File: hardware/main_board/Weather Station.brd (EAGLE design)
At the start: 55.5 x 44.4 mm, 34 parts, among them J2 RJ12, Q1 200mA/40V, Q2 220mA/50V/3.5Ω, U1 328P, U2 MCP1703T-3302E/CB, U3 W25X40CLSNIG, X2 B2B-PH-K-S, X3 B2B-XH-2, Y1 8MHz

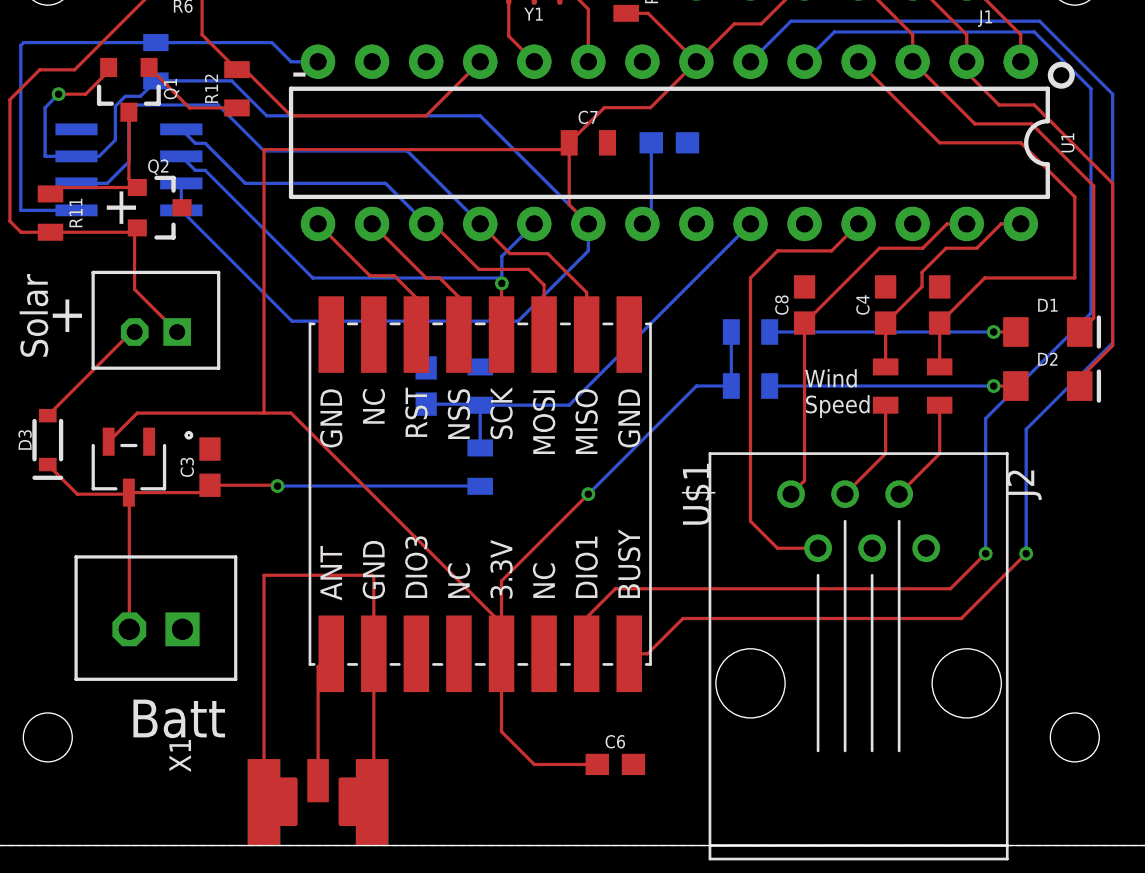
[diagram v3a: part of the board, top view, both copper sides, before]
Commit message: Added stationID to EEPROM and made changeable. Some hardware work.
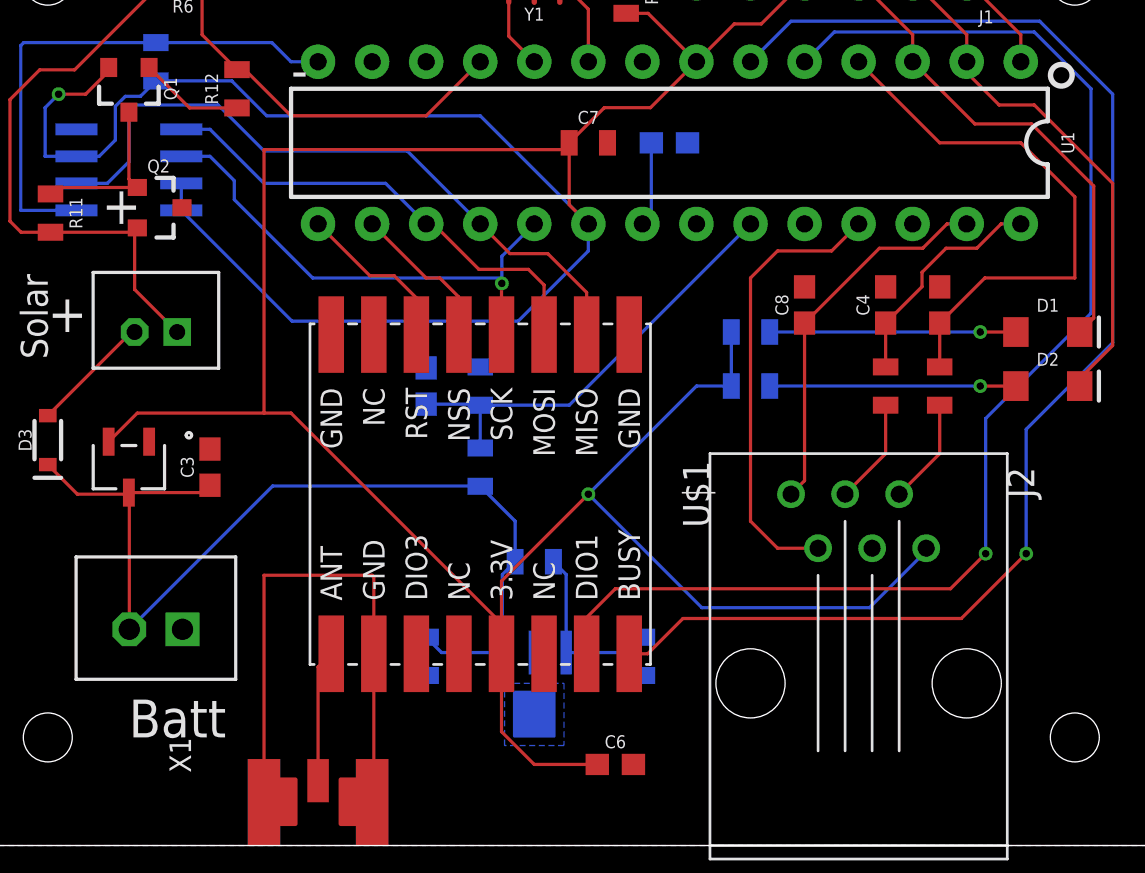
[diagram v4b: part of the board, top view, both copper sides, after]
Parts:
- added C9: 22uF, SparkFun-Capacitors:0805
- added R13, R7: (no value), SparkFun-Resistors:0805
- added U4: TL431BQPK, my-components:PK3
- C3: value 1.0uF -> 10uF
- R12: value 1k -> 33k
- R6: value 100k -> 10k
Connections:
- new net N$1: R13.1, R7.2, U4.3
- net GND: now also C9.2, R13.2, U4.2, U4.A2
- net VCC: now also J2.6
- net VIN: now also C9.1, R7.1, U4.1
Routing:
- net VCC: track 166.0 -> 185.3 mm
- net VIN: track 27.5 -> 46.7 mm, vias 1 -> 0
- net N$1: track 0.00 -> 8.39 mm
- net SCK: track 23.3 -> 23.8 mm
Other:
- board text added: "GND"
- board text added: "Sense Switch"
- board text added: "Shunt Voltage Reg"
- board text added: "Temp"
- board text added: "VCC"
- board text added: "Wind Dir"
- board text added: "Wind Spd"
- board text removed: "Wind Speed"

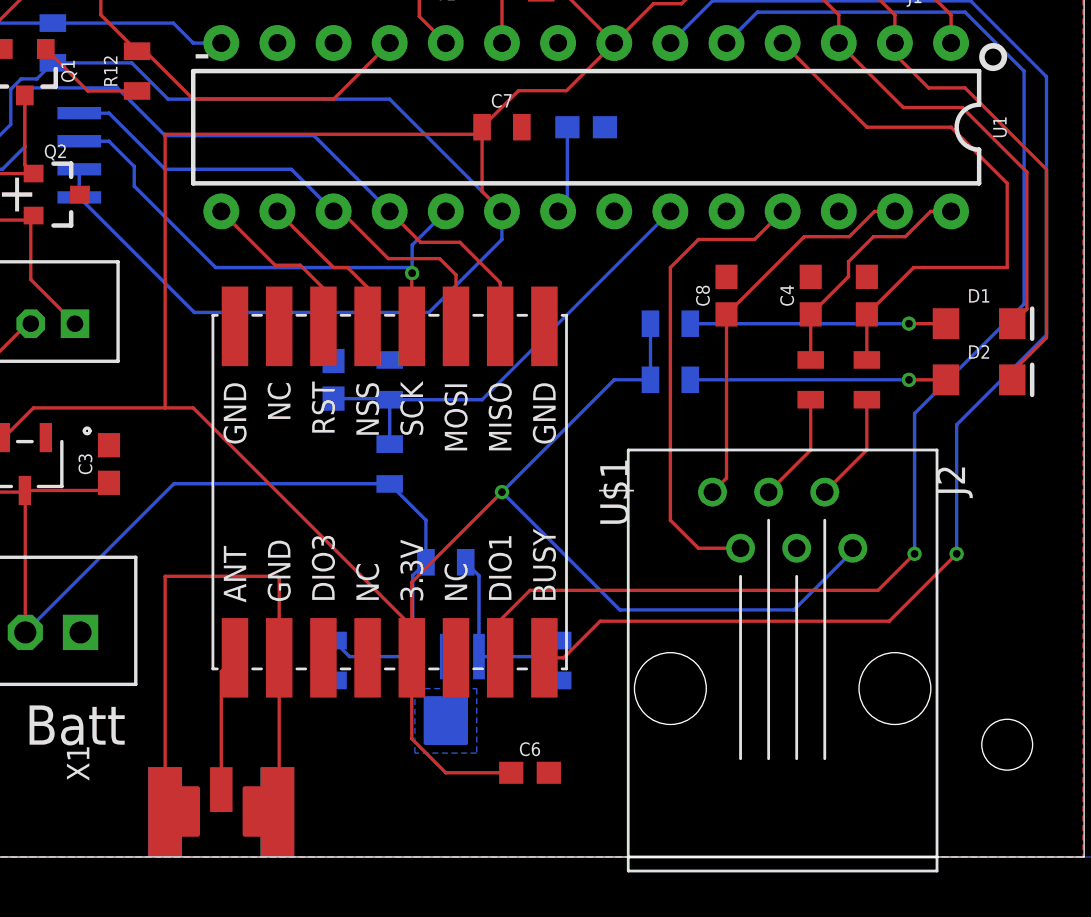
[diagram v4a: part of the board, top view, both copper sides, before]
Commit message: Switched to DRF126xT module
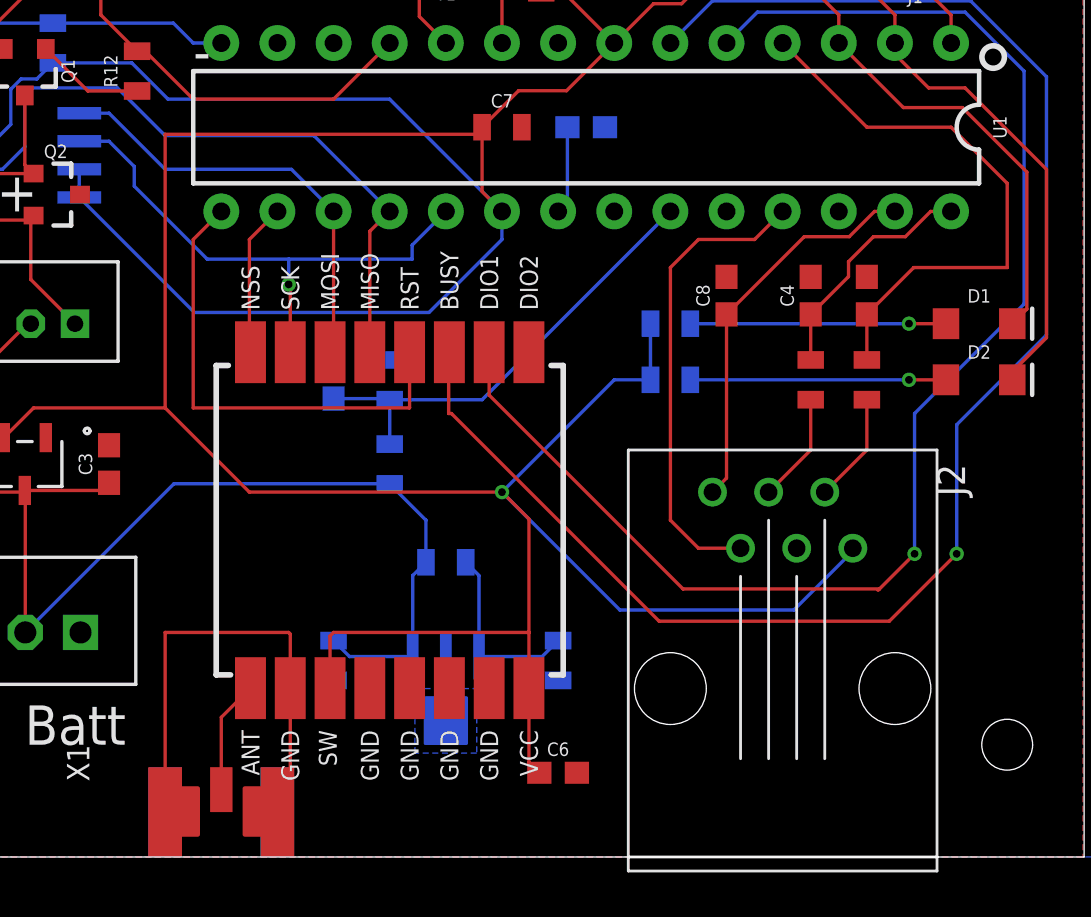
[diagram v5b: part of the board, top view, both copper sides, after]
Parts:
- U$1: value NICERF_SX1268 -> SX1262; device diy-modules:WIRELESS-LORA-NICERF1268 -> RadioShield:SX1262
- moved U$1 1.27 mm to (24.1, 15.2), turned to 90 degrees
- moved C6 1.27 mm to (31.8, 3.81)
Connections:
- net ANT: now also U$1.ANT; no longer U$1.B8
- net BUSY: now also U$1.BUSY; no longer U$1.B1
- net DIO1: now also U$1.DIO1; no longer U$1.B2
- net GND: now also U$1.GND@2, U$1.GND@3, U$1.GND@4, U$1.GND@5; no longer U$1.A1, U$1.A8
- net MISO: now also U$1.MISO; no longer U$1.A2
- net MOSI: now also U$1.MOSI; no longer U$1.A3
- net RF_GND: now also U$1.GND@1; no longer U$1.B7
- net SCK: now also U$1.SCK; no longer U$1.A4
- net SX_NSS: now also U$1.NSS; no longer U$1.A5
- net SX_RST: now also U$1.RST; no longer U$1.A6
- net VCC: now also U$1.SW, U$1.VCC; no longer U$1.B4
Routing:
- net SX_RST: track 7.78 -> 21.7 mm
- net BUSY: track 63.1 -> 73.4 mm
- net VCC: track 185.3 -> 191.7 mm
- net RF_GND: track 26.5 -> 22.1 mm
- net DIO1: track 60.7 -> 64.6 mm
- net MOSI: track 22.4 -> 20.1 mm
- net MISO: track 32.7 -> 31.1 mm
- net ANT: track 6.22 -> 5.14 mm
- net SCK: track 23.8 -> 24.8 mm

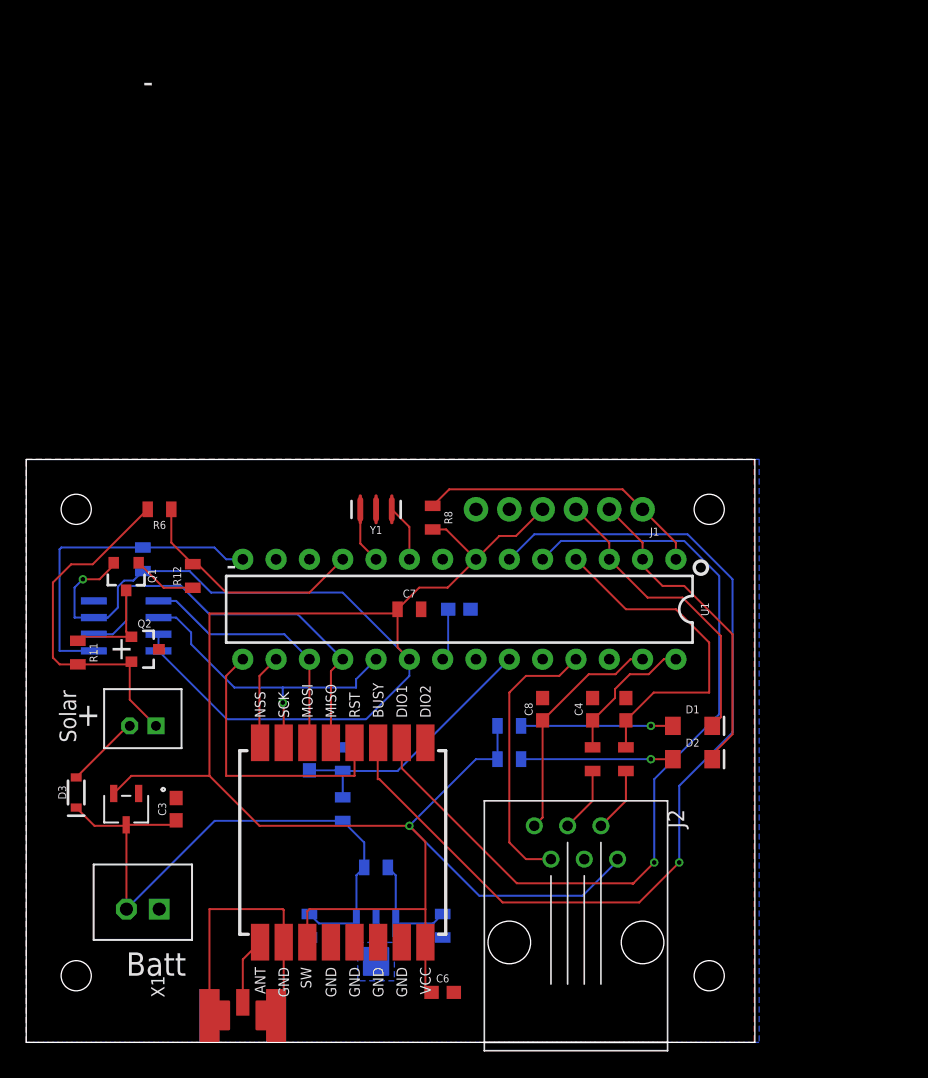
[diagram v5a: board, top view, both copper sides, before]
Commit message: Better speed formatting for null values; Some other stuff
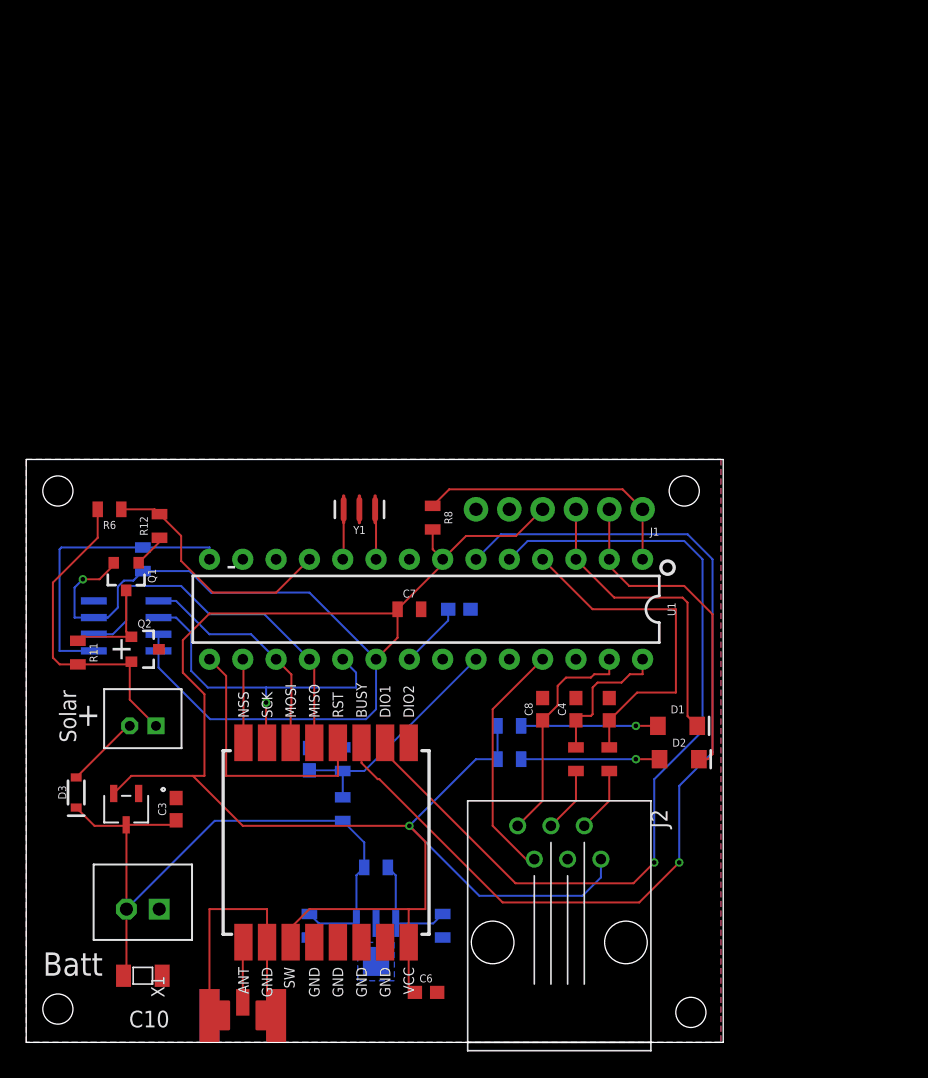
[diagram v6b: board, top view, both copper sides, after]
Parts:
- added C10: 100uF, capsmd:1206
- moved R12 4.58 mm to (10.2, 39.4)
- moved R6 3.81 mm to (6.35, 40.6)
- moved U1 2.54 mm to (30.5, 33.0)
- moved C4 1.27 mm to (41.9, 25.4)
- moved R1 1.27 mm to (41.9, 21.6)
- moved Y1 1.27 mm to (25.4, 40.6)
- moved C6 1.27 mm to (30.5, 3.81)
- moved U$1 1.27 mm to (22.9, 15.2)
- moved C2 1.27 mm to (44.5, 25.4)
- moved J2 1.27 mm to (40.6, 7.62)
- moved R2 1.27 mm to (44.5, 21.6)
- moved D1 1.14 mm to (49.7, 24.1)
- moved D2 1.02 mm to (49.8, 21.6)
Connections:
- net GND: now also C10.1
- net VIN: now also C10.2
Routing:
- net VIN: track 46.7 -> 51.9 mm
- net MISO: track 31.1 -> 28.4 mm
- net WINDDIR_PWR: track 21.3 -> 18.5 mm
- net BATT_SENSE: track 20.8 -> 18.3 mm
- net N$9: track 27.2 -> 24.6 mm
- net MOSI: track 20.1 -> 17.7 mm
- net N$13: track 4.92 -> 2.57 mm
- net FLASH_SS: track 24.8 -> 22.8 mm
- net DIO1: track 64.6 -> 66.6 mm
- net BUSY: track 73.4 -> 75.2 mm
- net VCC: track 191.7 -> 190.2 mm
- net SX_RST: track 21.7 -> 20.5 mm
- net RF_GND: track 22.1 -> 20.9 mm
- net N$4: track 11.6 -> 10.4 mm
- net AT_RST: track 22.0 -> 21.0 mm
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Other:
- board size 55.5 x 44.4 mm -> 53.1 x 44.4 mm

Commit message: ALS Wind direction bug fixes. Added ability to chain receivers using UDP. QueryVolatileResponse bugfix.
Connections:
- net TEMP_SENSE renamed TEMP_SENSE_SDA
- net WINDDIR_PWR renamed WINDDIR_PWR_TS2
- net WINDDIR_SENSE renamed WINDDIR_SENSE_SCL
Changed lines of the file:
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@@
 <wire x1="32.247" y1="42.164" x2="45.466" y2="42.164" width="0.1524" layer="1"/>
 </signal>
-<signal name="WINDDIR_PWR">
+<signal name="WINDDIR_PWR_TS2">
 <contactref element="U1" pad="25"/>
 <contactref element="J2" pad="2"/>
@@
 <contactref element="X1" pad="GND@4"/>
 </signal>
-<signal name="WINDDIR_SENSE">
+<signal name="WINDDIR_SENSE_SCL">
 <contactref element="C4" pad="1"/>
 <contactref element="R1" pad="1"/>
@@
 <wire x1="8.89" y1="37.73" x2="13.97" y2="37.73" width="0.1524" layer="16"/>
 </signal>
-<signal name="TEMP_SENSE">
+<signal name="TEMP_SENSE_SDA">
 <contactref element="J2" pad="1"/>
 <contactref element="U1" pad="27"/>
